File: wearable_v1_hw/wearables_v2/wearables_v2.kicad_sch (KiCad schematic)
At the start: 40 parts, among them IC1 STM32WB05KZV6TR, IC2 TPS7A0228PDBVR, J1 217175-0001, J2 Conn_01x03, J3 Conn_01x04, Q1 PMOS, SW1 Reset, U1 DLF162500LT-5028A1, U2 2450AT18A100E, U3 BMI270, U5 MCP73831-2-MC, Y1 ABM10W-32.0000MHZ-8-B1U-T3, Y2 Crystal

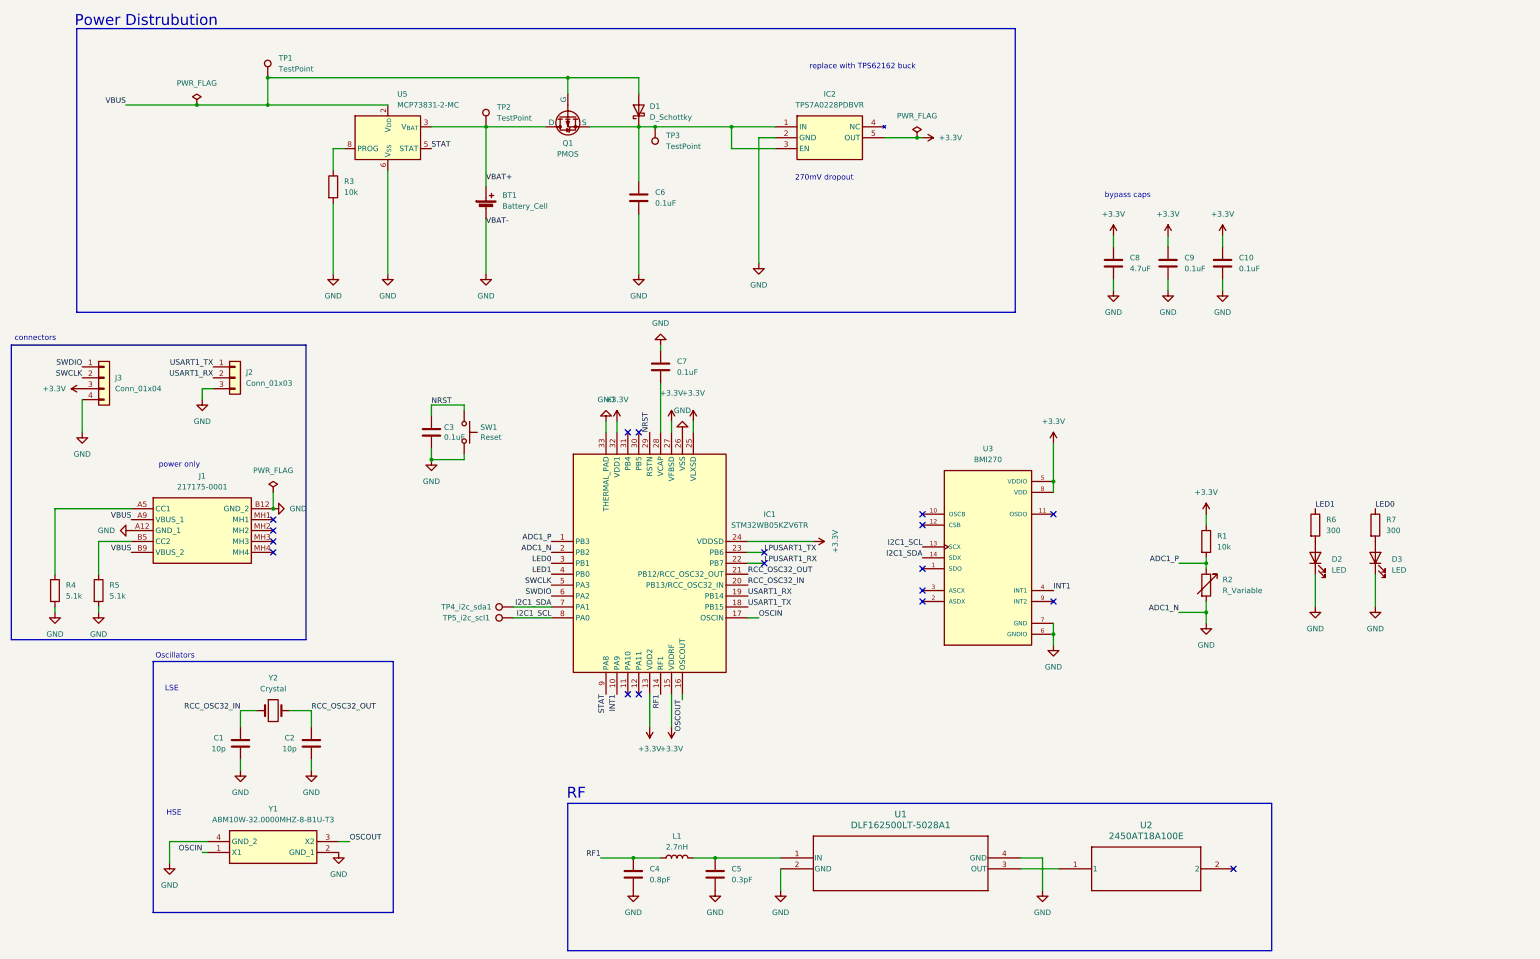
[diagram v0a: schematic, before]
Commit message: new nrf variant
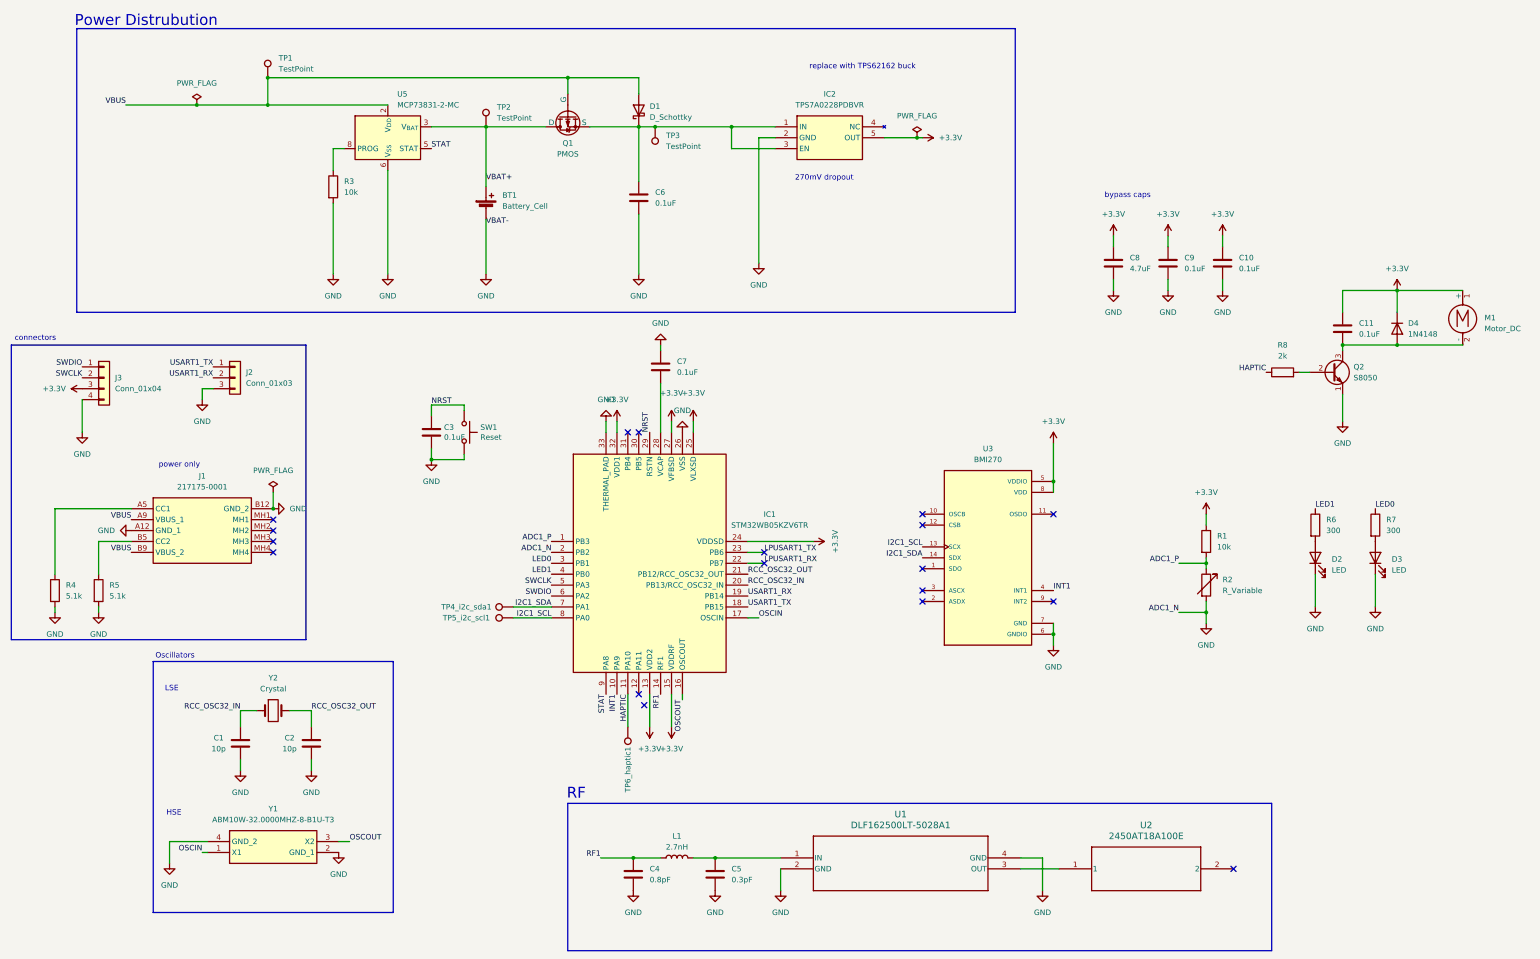
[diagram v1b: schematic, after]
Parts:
- added C11: 0.1uF, Capacitor_SMD:C_0805_2012Metric, symbol Device:C
- added D4: 1N4148, Diode_THT:D_DO-35_SOD27_P7.62mm_Horizontal, symbol Diode:1N4148
- added M1: Motor_DC, Connector_PinHeader_2.54mm:PinHeader_1x02_P2.54mm_Vertical, symbol Motor:Motor_DC
- added Q2: S8050, Package_TO_SOT_THT:TO-92_Inline, symbol Transistor_BJT:S8050
- added R8: 2k, Resistor_SMD:R_0805_2012Metric, symbol Device:R
- added TP6_haptic1: TestPoint, A_wearables:5000, symbol Connector:TestPoint
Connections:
- net +3.3V: now also C11.1, D4.1 (K), M1.1 (+)
- net GND: now also Q2.1 (E)
- net HAPTIC: now reaches IC1.11 (PA10)
- net HAPTIC: now also R8.1, TP6_haptic1.1
- new net: Q2.2 (B), R8.2
- new net: C11.2, D4.2 (A), M1.2 (-), Q2.3 (C)

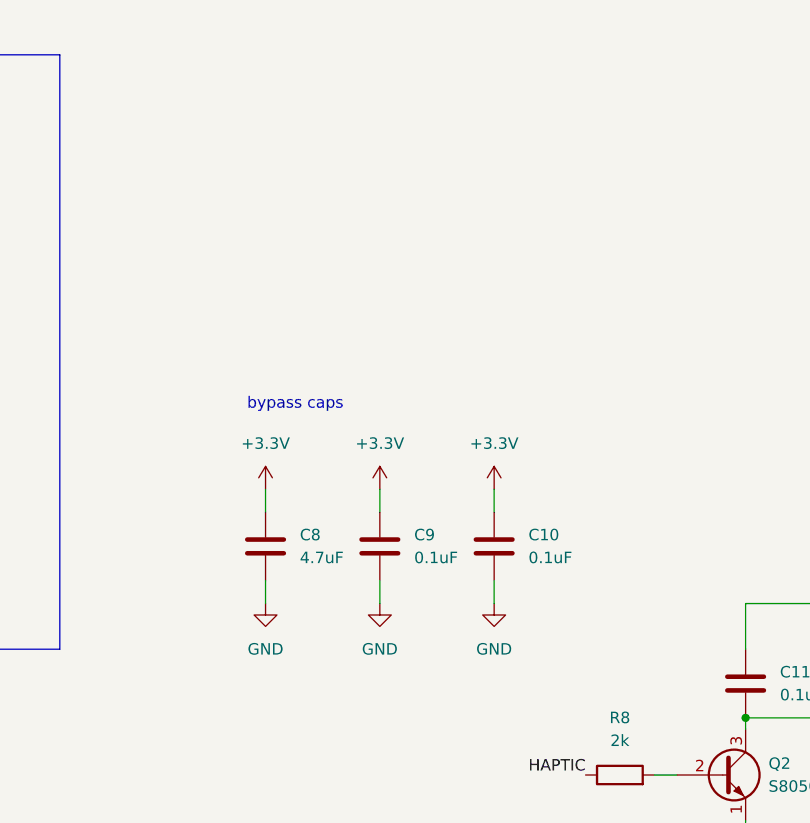
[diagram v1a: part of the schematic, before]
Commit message: finished nrf schematic/layout 👷‍♂️
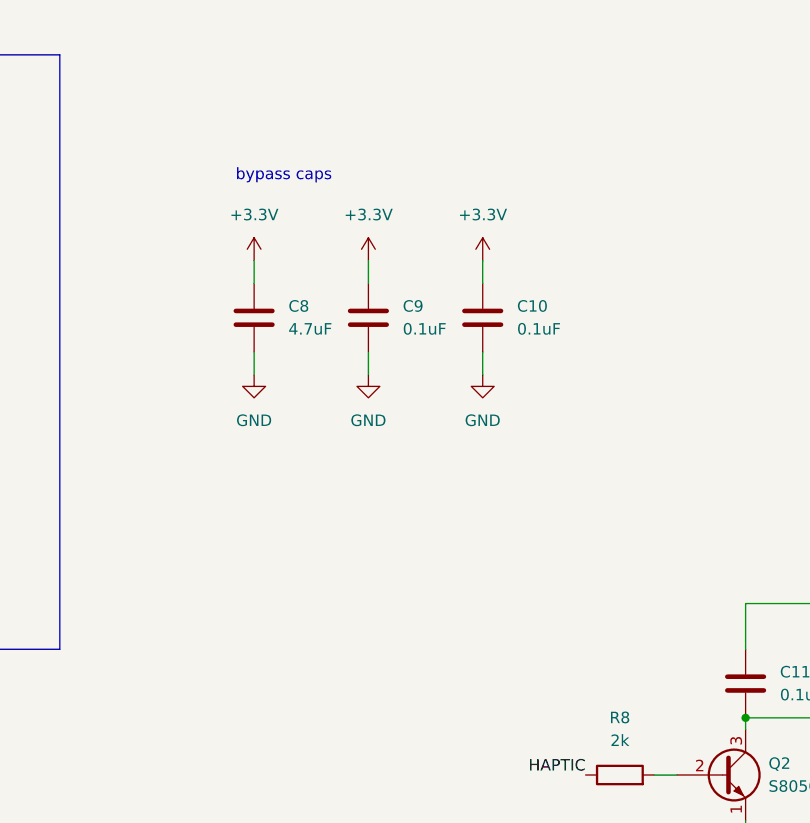
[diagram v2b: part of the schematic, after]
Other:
- moved on the sheet: C10, C8, C9
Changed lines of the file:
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@@
 	(wire
 		(pts
-			(xy 294.64 68.58) (xy 294.64 71.12)
+			(xy 293.37 43.18) (xy 293.37 45.72)
 		)
 		(stroke
@@
 	(wire
 		(pts
-			(xy 294.64 78.74) (xy 294.64 81.28)
+			(xy 293.37 53.34) (xy 293.37 55.88)
 		)
 		(stroke
@@
 	(wire
 		(pts
-			(xy 320.04 78.74) (xy 320.04 81.28)
+			(xy 318.77 53.34) (xy 318.77 55.88)
 		)
 		(stroke
@@
 	(wire
 		(pts
-			(xy 307.34 78.74) (xy 307.34 81.28)
+			(xy 306.07 53.34) (xy 306.07 55.88)
 		)
 		(stroke
@@
 	(wire
 		(pts
-			(xy 307.34 68.58) (xy 307.34 71.12)
+			(xy 306.07 43.18) (xy 306.07 45.72)
 		)
 		(stroke
@@
 	(wire
 		(pts
-			(xy 320.04 68.58) (xy 320.04 71.12)
+			(xy 318.77 43.18) (xy 318.77 45.72)
 		)
 		(stroke
@@
 	(text "bypass caps\n"
 		(exclude_from_sim no)
-		(at 297.942 59.182 0)
+		(at 296.672 33.782 0)
 		(effects
 			(font
@@
 	(symbol
 		(lib_id "Device:C")
-		(at 294.64 74.93 0)
+		(at 293.37 49.53 0)
 		(unit 1)
 		(exclude_from_sim no)
@@
 		(fields_autoplaced yes)
 		(property "Reference" "C8"
-			(at 298.45 73.6599 0)
+			(at 297.18 48.2599 0)
 			(effects
 				(font
@@
 		)
 		(property "Value" "4.7uF"
-			(at 298.45 76.1999 0)
+			(at 297.18 50.7999 0)
 			(effects
 				(font
@@
 		)
 		(property "Footprint" "Capacitor_SMD:C_0805_2012Metric"
-			(at 295.6052 78.74 0)
+			(at 294.3352 53.34 0)
 			(effects
 				(font
@@
 		)
 		(property "Datasheet" "~"
-			(at 294.64 74.93 0)
+			(at 293.37 49.53 0)
 			(effects
 				(font
@@
 		)
 		(property "Description" "Unpolarized capacitor"
-			(at 294.64 74.93 0)
+			(at 293.37 49.53 0)
 			(effects
 				(font
@@
 	(symbol
 		(lib_id "power:+3.3V")
-		(at 320.04 68.58 0)
+		(at 318.77 43.18 0)
 		(unit 1)
 		(exclude_from_sim no)
@@
 		(fields_autoplaced yes)
 		(property "Reference" "#PWR041"
-			(at 320.04 72.39 0)
+			(at 318.77 46.99 0)
 			(effects
 				(font
@@
 		)
 		(property "Value" "+3.3V"
-			(at 320.04 63.5 0)
+			(at 318.77 38.1 0)
 			(effects
 				(font
@@
 		)
 		(property "Footprint" ""
-			(at 320.04 68.58 0)
+			(at 318.77 43.18 0)
 			(effects
 				(font
@@
 		)
 		(property "Datasheet" ""
-			(at 320.04 68.58 0)
+			(at 318.77 43.18 0)
 			(effects
 				(font
@@
 		)
 		(property "Description" "Power symbol creates a global label with name \"+3.3V\""
-			(at 320.04 68.58 0)
+			(at 318.77 43.18 0)
 			(effects
 				(font
@@
 	(symbol
 		(lib_id "power:+3.3V")
-		(at 307.34 68.58 0)
+		(at 306.07 43.18 0)
 		(unit 1)
 		(exclude_from_sim no)
@@
 		(fields_autoplaced yes)
 		(property "Reference" "#PWR039"
-			(at 307.34 72.39 0)
+			(at 306.07 46.99 0)
 			(effects
 				(font
@@
 		)
 		(property "Value" "+3.3V"
-			(at 307.34 63.5 0)
+			(at 306.07 38.1 0)
 			(effects
 				(font
@@
 		)
 		(property "Footprint" ""
-			(at 307.34 68.58 0)
+			(at 306.07 43.18 0)
 			(effects
 				(font
@@
 		)
 		(property "Datasheet" ""
-			(at 307.34 68.58 0)
+			(at 306.07 43.18 0)
 			(effects
 				(font
@@
 		)
 		(property "Description" "Power symbol creates a global label with name \"+3.3V\""
-			(at 307.34 68.58 0)
+			(at 306.07 43.18 0)
 			(effects
 				(font
@@
 		(lib_name "GND_1")
 		(lib_id "power:GND")
-		(at 294.64 81.28 0)
+		(at 293.37 55.88 0)
 		(unit 1)
 		(exclude_from_sim no)
@@
 		(fields_autoplaced yes)
 		(property "Reference" "#PWR038"
-			(at 294.64 87.63 0)
+			(at 293.37 62.23 0)
 			(effects
 				(font
@@
 		)
 		(property "Value" "GND"
-			(at 294.64 86.36 0)
+			(at 293.37 60.96 0)
 			(effects
 				(font
@@
 		)
 		(property "Footprint" ""
-			(at 294.64 81.28 0)
+			(at 293.37 55.88 0)
 			(effects
 				(font
@@
 		)
 		(property "Datasheet" ""
-			(at 294.64 81.28 0)
+			(at 293.37 55.88 0)
 			(effects
 				(font
@@
 		)
 		(property "Description" "Power symbol creates a global label with name \"GND\" , ground"
-			(at 294.64 81.28 0)
+			(at 293.37 55.88 0)
 			(effects
 				(font
@@
 	(symbol
 		(lib_id "power:+3.3V")
-		(at 294.64 68.58 0)
+		(at 293.37 43.18 0)
 		(unit 1)
 		(exclude_from_sim no)
@@
 		(fields_autoplaced yes)
 		(property "Reference" "#PWR037"
-			(at 294.64 72.39 0)
+			(at 293.37 46.99 0)
 			(effects
 				(font
@@
 		)
 		(property "Value" "+3.3V"
-			(at 294.64 63.5 0)
+			(at 293.37 38.1 0)
 			(effects
 				(font
@@
 		)
 		(property "Footprint" ""
-			(at 294.64 68.58 0)
+			(at 293.37 43.18 0)
 			(effects
 				(font
@@
 		)
 		(property "Datasheet" ""
-			(at 294.64 68.58 0)
+			(at 293.37 43.18 0)
 			(effects
 				(font
@@
 		)
 		(property "Description" "Power symbol creates a global label with name \"+3.3V\""
-			(at 294.64 68.58 0)
+			(at 293.37 43.18 0)
 			(effects
 				(font
@@
 	(symbol
 		(lib_id "Device:C")
-		(at 320.04 74.93 0)
+		(at 318.77 49.53 0)
 		(unit 1)
 		(exclude_from_sim no)
@@
 		(fields_autoplaced yes)
 		(property "Reference" "C10"
-			(at 323.85 73.6599 0)
+			(at 322.58 48.2599 0)
 			(effects
 				(font
@@
 		)
 		(property "Value" "0.1uF"
-			(at 323.85 76.1999 0)
+			(at 322.58 50.7999 0)
 			(effects
 				(font
@@
 		)
 		(property "Footprint" "Capacitor_SMD:C_0805_2012Metric"
-			(at 321.0052 78.74 0)
+			(at 319.7352 53.34 0)
 			(effects
 				(font
@@
 		)
 		(property "Datasheet" "~"
-			(at 320.04 74.93 0)
+			(at 318.77 49.53 0)
 			(effects
 				(font
@@
 		)
 		(property "Description" "Unpolarized capacitor"
-			(at 320.04 74.93 0)
+			(at 318.77 49.53 0)
 			(effects
 				(font
@@
 		(lib_name "GND_1")
 		(lib_id "power:GND")
-		(at 320.04 81.28 0)
+		(at 318.77 55.88 0)
 		(unit 1)
 		(exclude_from_sim no)
@@
 		(fields_autoplaced yes)
 		(property "Reference" "#PWR042"
-			(at 320.04 87.63 0)
+			(at 318.77 62.23 0)
 			(effects
 				(font
@@
 		)
 		(property "Value" "GND"
-			(at 320.04 86.36 0)
+			(at 318.77 60.96 0)
 			(effects
 				(font
@@
 		)
 		(property "Footprint" ""
-			(at 320.04 81.28 0)
+			(at 318.77 55.88 0)
 			(effects
 				(font
@@
 		)
 		(property "Datasheet" ""
-			(at 320.04 81.28 0)
+			(at 318.77 55.88 0)
 			(effects
 				(font
@@
 		)
 		(property "Description" "Power symbol creates a global label with name \"GND\" , ground"
-			(at 320.04 81.28 0)
+			(at 318.77 55.88 0)
 			(effects
 				(font
@@
 	(symbol
 		(lib_id "Device:C")
-		(at 307.34 74.93 0)
+		(at 306.07 49.53 0)
 		(unit 1)
 		(exclude_from_sim no)
@@
 		(fields_autoplaced yes)
 		(property "Reference" "C9"
-			(at 311.15 73.6599 0)
+			(at 309.88 48.2599 0)
 			(effects
 				(font
@@
 		)
 		(property "Value" "0.1uF"
-			(at 311.15 76.1999 0)
+			(at 309.88 50.7999 0)
 			(effects
 				(font
@@
 		)
 		(property "Footprint" "Capacitor_SMD:C_0805_2012Metric"
-			(at 308.3052 78.74 0)
+			(at 307.0352 53.34 0)
 			(effects
 				(font
@@
 		)
 		(property "Datasheet" "~"
-			(at 307.34 74.93 0)
+			(at 306.07 49.53 0)
 			(effects
 				(font
@@
 		)
 		(property "Description" "Unpolarized capacitor"
-			(at 307.34 74.93 0)
+			(at 306.07 49.53 0)
 			(effects
 				(font
@@
 		(lib_name "GND_1")
 		(lib_id "power:GND")
-		(at 307.34 81.28 0)
+		(at 306.07 55.88 0)
 		(unit 1)
 		(exclude_from_sim no)
@@
 		(fields_autoplaced yes)
 		(property "Reference" "#PWR040"
-			(at 307.34 87.63 0)
+			(at 306.07 62.23 0)
 			(effects
 				(font
@@
 		)
 		(property "Value" "GND"
-			(at 307.34 86.36 0)
+			(at 306.07 60.96 0)
 			(effects
 				(font
@@
 		)
 		(property "Footprint" ""
-			(at 307.34 81.28 0)
+			(at 306.07 55.88 0)
 			(effects
 				(font
@@
 		)
 		(property "Datasheet" ""
-			(at 307.34 81.28 0)
+			(at 306.07 55.88 0)
 			(effects
 				(font
@@
 		)
 		(property "Description" "Power symbol creates a global label with name \"GND\" , ground"
-			(at 307.34 81.28 0)
+			(at 306.07 55.88 0)
 			(effects
 				(font
